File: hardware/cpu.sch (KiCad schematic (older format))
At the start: 6 parts

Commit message: Partial updates for hardware revision 2
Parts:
- removed U?: 74HCT245, symbol 74xx:74HC245
- removed U?: 74AC573, symbol 74xx:74LS573
- removed U?: CAD2, Package_DIP:DIP-24_W7.62mm_Socket, symbol custom_chips:CAD
- removed U?: CID, Package_DIP:DIP-24_W7.62mm_Socket, symbol custom_chips:CBD
- added C? (x5): 0.1uf, symbol Device:C_Small
- added J?: JTAG, Connector_IDC:IDC-Header_2x05_P2.54mm_Vertical, symbol Connector:Conn_ARM_JTAG_SWD_10
- added U? (x3): SN74HC21N, symbol 74xx:74LS21
- added U?: CSC, Package_QFP:TQFP-44_10x10mm_P0.8mm, symbol custom_chips:CSC
- RN?: value R_Network06_US -> 4607X-101-332LF
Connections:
- net labels added: +3V3, R~W, SPI65_TDI, TCK, TDI, TDO, TMS, ~ABORT, ~INTR1, ~INTR2, ~INTR3, ~INTR4, ~IOSEL1, ~IOSEL2, ~IOSEL3, ~IOSEL4, ~IRQ, ~NMI, ~RAM1CS, ~RAM2CS, ~RD, ~RESET, ~ROMCS, ~WR, ϕ2
- net labels removed: +5V, A19, A20, A21, A22, A23, ABORT, INTR1B, INTR2B, INTR3B, INTR4B, IO1SELB, IO2SELB, IO3SELB, IO4SELB, IRQ, IRQB, NMI, PHI1, PHI2, RAM1CSB, RAM2CSB, RDB, RESB, RESET, ROMCSB, ROMPROT, ROMWRB, RWB, WRB
- wire segments 128 -> 136
- no-connect marks 4 -> 6
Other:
- moved on the sheet: RN?, U?

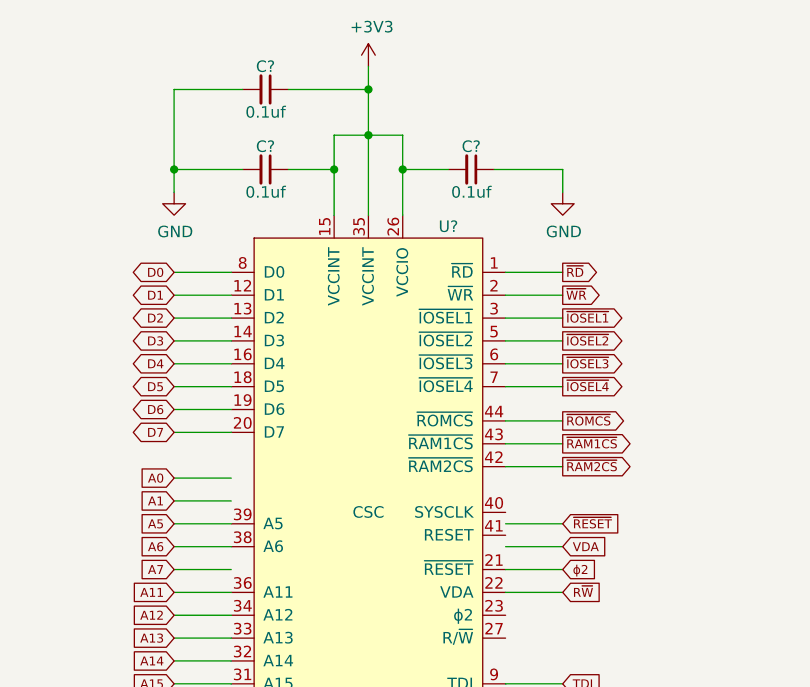
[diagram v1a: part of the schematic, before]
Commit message: Add SPI and missing caps on MAX3232s.
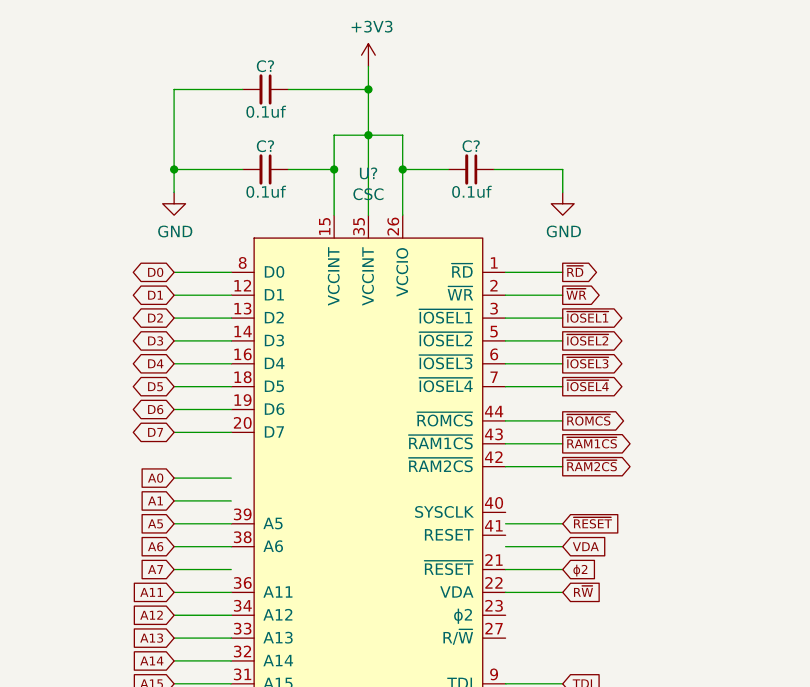
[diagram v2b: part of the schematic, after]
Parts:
- removed U?: CSC, Package_QFP:TQFP-44_10x10mm_P0.8mm, symbol custom_chips:CSC
- added U?: CSC, Package_QFP:TQFP-44_10x10mm_P0.8mm, symbol custom_chips:CSC
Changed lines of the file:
@@
 ~RESET
-$Comp
-L custom_chips:CSC U?
-U 1 1 5DF7979C
-P 6550 2900
-F 0 "U?" H 6900 4150 50  0000 C CNN
-F 1 "CSC" H 6550 2900 50  0000 C CNN
-F 2 "Package_QFP:TQFP-44_10x10mm_P0.8mm" H 6550 2850 50  0001 C CNN
-F 3 "https://www.xilinx.com/support/documentation/data_sheets/ds057.pdf" H 6550 2850 50  0001 C CNN
-	1    6550 2900
-	1    0    0    -1
-$EndComp
 $Comp
 L power:+3V3 #PWR?
@@
 Text GLabel 8850 3650 0    39   Input ~ 0
 TDO
+$Comp
+L custom_chips:CSC U?
+U 1 1 5E4F0787
+P 6550 2900
+F 0 "U?" H 6550 4381 50  0000 C CNN
+F 1 "CSC" H 6550 4290 50  0000 C CNN
+F 2 "Package_QFP:TQFP-44_10x10mm_P0.8mm" H 6550 2850 50  0001 C CNN
+F 3 "https://www.xilinx.com/support/documentation/data_sheets/ds057.pdf" H 6550 2850 50  0001 C CNN
+	1    6550 2900
+	1    0    0    -1
+$EndComp
 $EndSCHEMATC

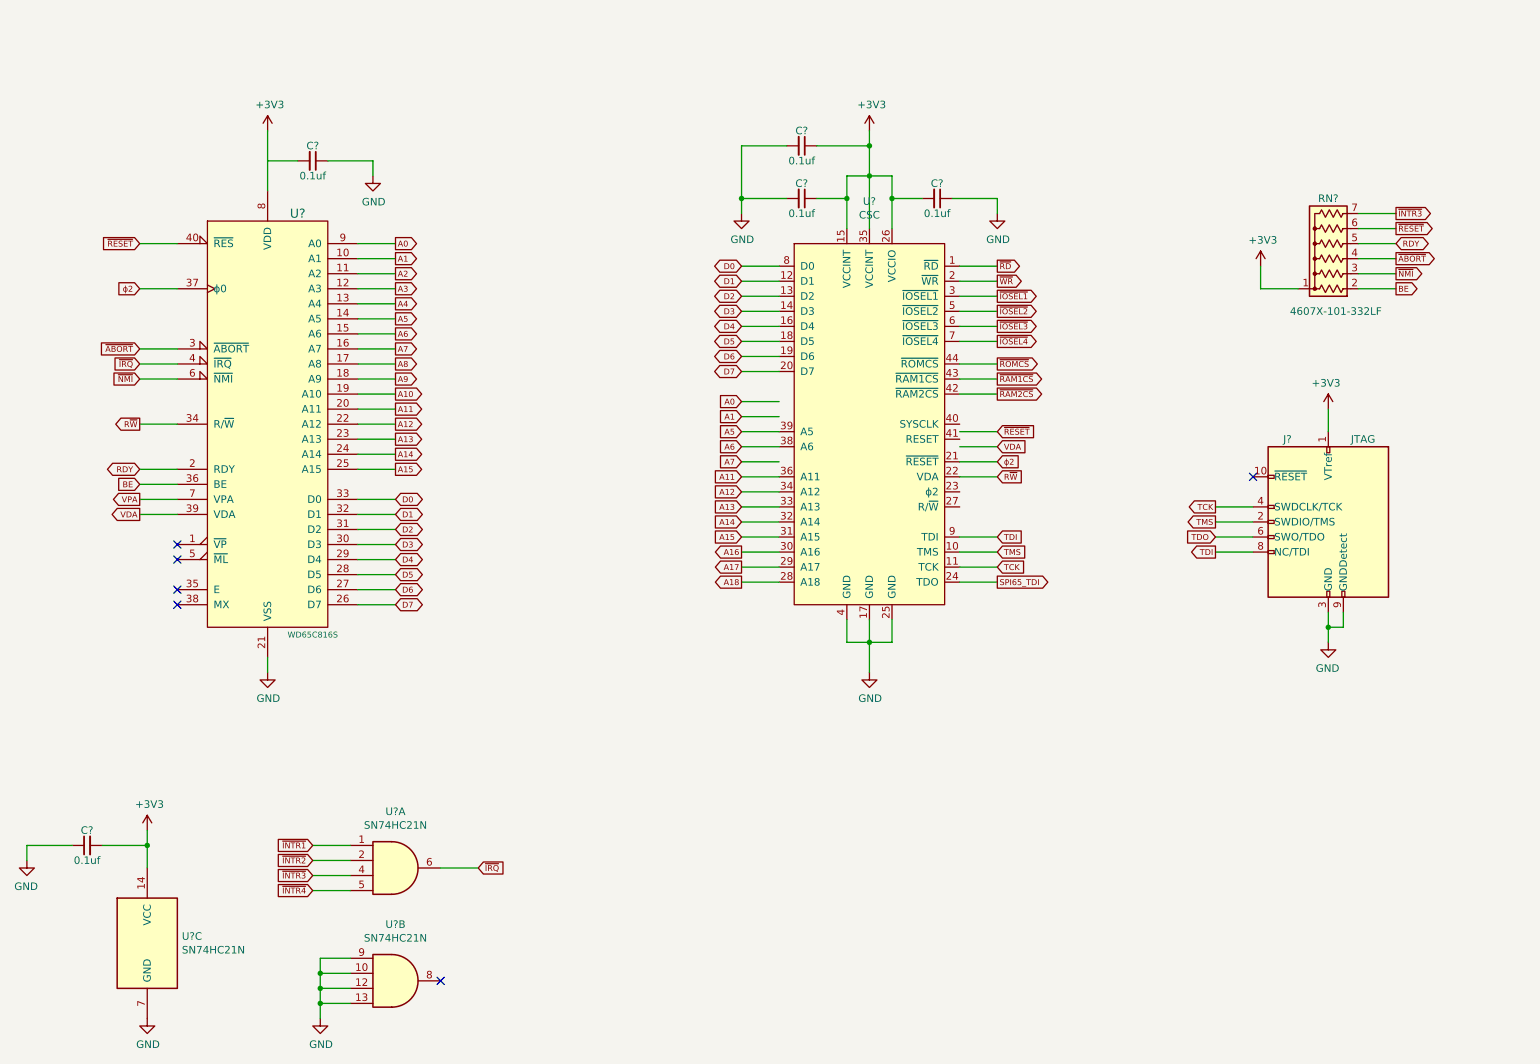
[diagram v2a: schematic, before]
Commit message: Combine VIA, SPI, and UART into a single io.sch sheet. The serial.sch sheet is now just the serial ports and the line drivers.
Add ports.sch sheet for remaining I/O ports.
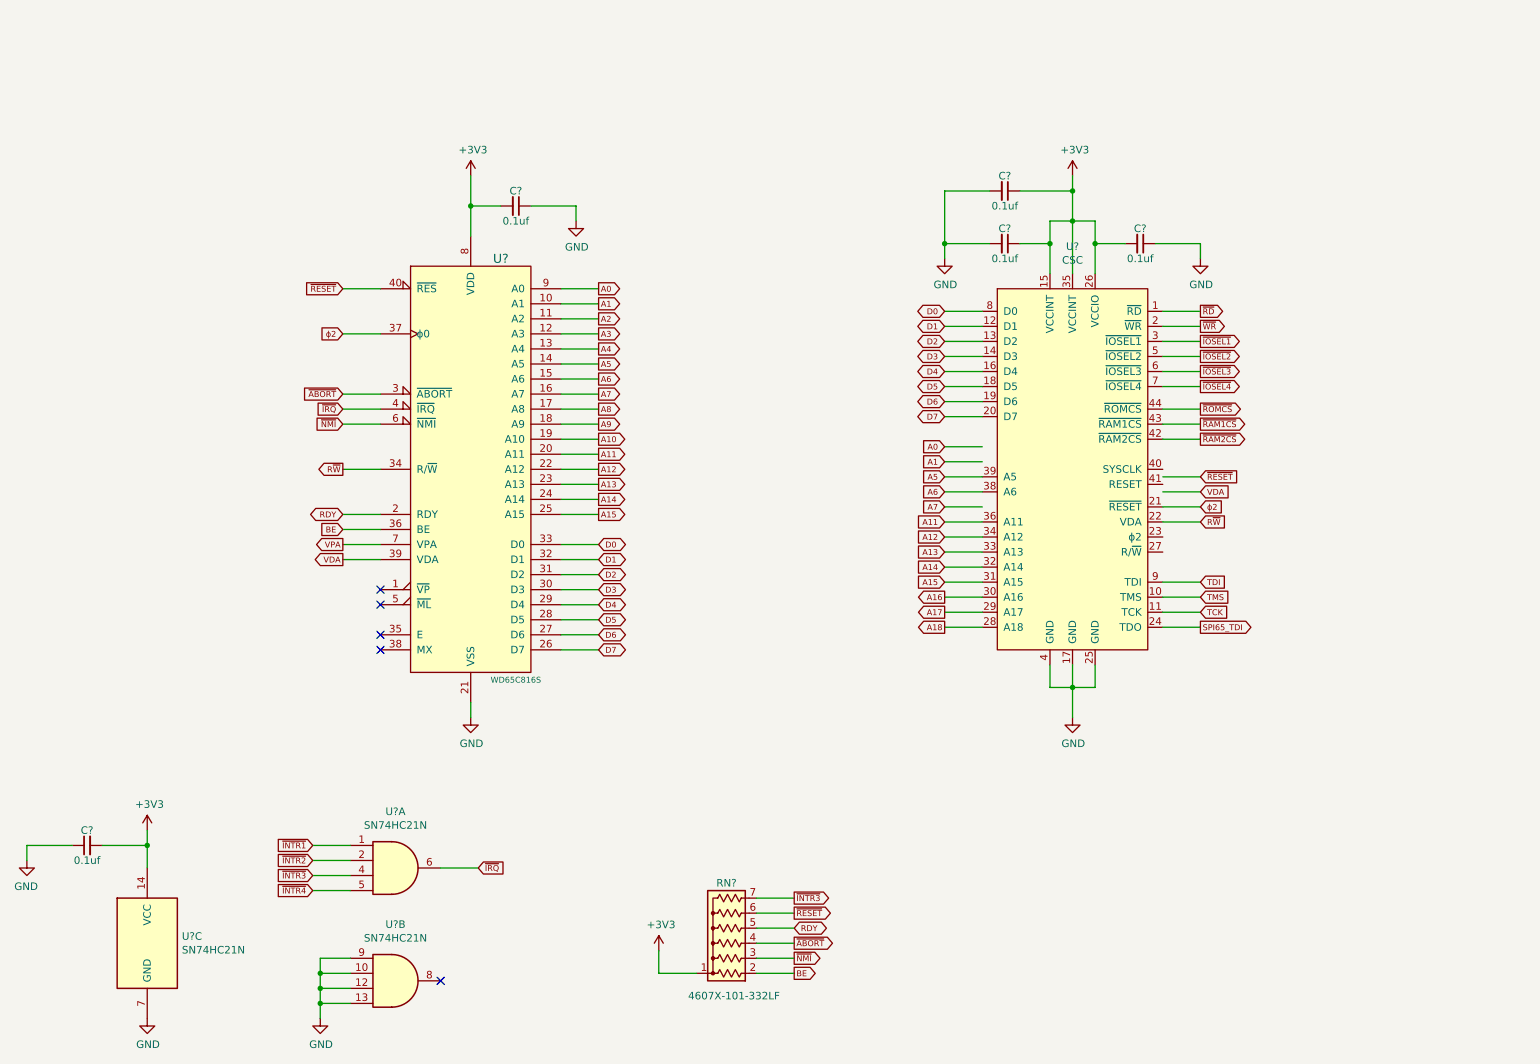
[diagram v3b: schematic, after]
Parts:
- removed J?: JTAG, Connector_IDC:IDC-Header_2x05_P2.54mm_Vertical, symbol Connector:Conn_ARM_JTAG_SWD_10
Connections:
- net labels removed: TDO
- wire segments 136 -> 128
- no-connect marks 6 -> 5
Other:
- moved on the sheet: C?, RN?, U?

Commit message: Latest schematic
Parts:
- RN?: value 4607X-101-332LF -> 4608X-101-332LF; footprint Resistor_THT:R_Array_SIP7 -> Resistor_THT:R_Array_SIP8; symbol Device:R_Network06_US -> Device:R_Network07_US
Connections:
- net ~INTR3: now also RN?.8 (R7); no longer RN?.7 (R6)
- new net RESET: RN?.7 (R6)
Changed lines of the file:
@@
 $Descr A4 11693 8268
 encoding utf-8
-Sheet 2 7
+Sheet 2 8
 Title "CPU and System Controller"
 Date ""
@@
 	3300 3700 3050 3700
 $Comp
-L Device:R_Network06_US RN?
+L Device:R_Network07_US RN?
 U 1 1 5BAB6B12
 P 5600 6250
 F 0 "RN?" V 5900 6250 50  0000 C CNN
-F 1 "4607X-101-332LF" V 5150 6200 50  0000 C CNN
-F 2 "Resistor_THT:R_Array_SIP7" V 5975 6250 50  0001 C CNN
+F 1 "4608X-101-332LF" V 5150 6200 50  0000 C CNN
+F 2 "Resistor_THT:R_Array_SIP8" V 5975 6250 50  0001 C CNN
 F 3 "https://www.mouser.com/datasheet/2/54/4600x-776645.pdf" H 5600 6250 50  0001 C CNN
 	1    5600 6250
 	0    -1   -1   0
 $EndComp
-Text GLabel 6050 6050 2    39   Output ~ 0
+Text GLabel 6050 5950 2    39   Output ~ 0
 ~INTR3
 Wire Wire Line
-	5800 6050 6050 6050
+	5800 5950 6050 5950
 $Comp
 L power:GND #PWR?
@@
 Wire Wire Line
 	3900 1450 3900 1650
+Wire Wire Line
+	5800 6050 6050 6050
+Text GLabel 6050 6050 2    39   Output ~ 0
+RESET
 $EndSCHEMATC

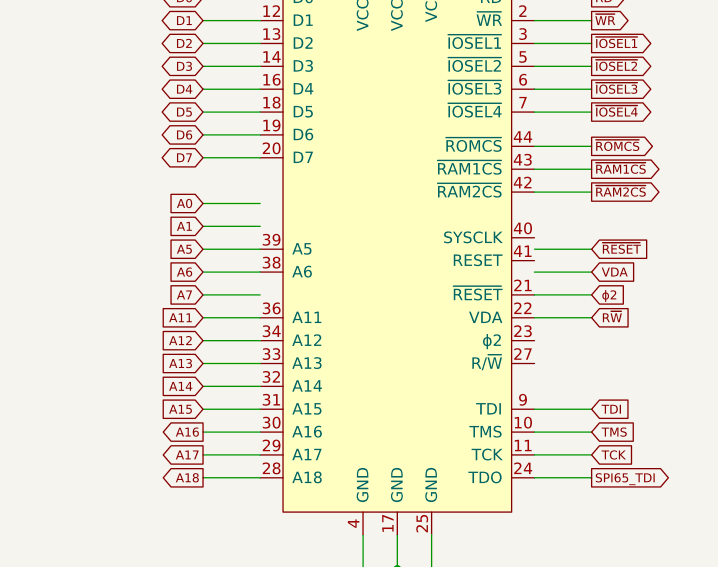
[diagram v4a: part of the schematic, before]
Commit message: More schematic updates to match current prototype build
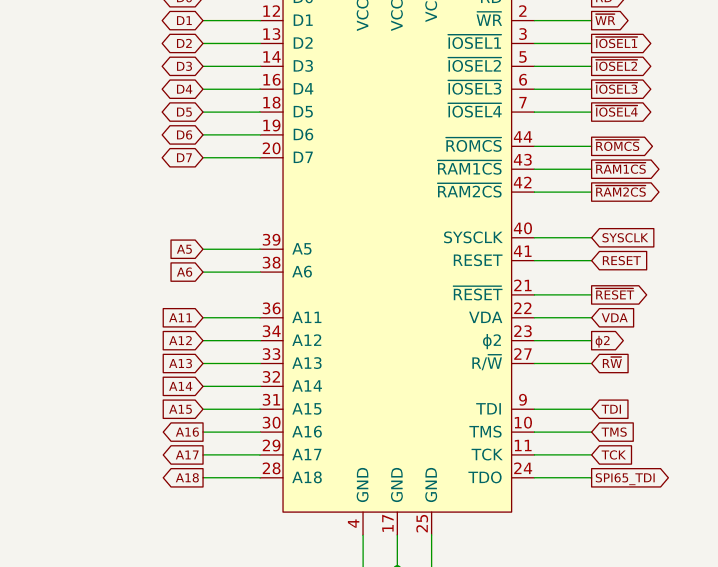
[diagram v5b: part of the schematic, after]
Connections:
- net A7: no longer U?.37 (unused)
- net RESET: now also U?.41 (RESET)
- net R~W: now also U?.27 (R/~W); no longer U?.22 (VDA)
- net VDA: now also U?.22 (VDA)
- net ~RESET: now also U?.21 (~RESET)
- net ϕ2: now also U?.23 (ϕ2); no longer U?.21 (~RESET)
- net SYSCLK: now reaches U?.40 (SYSCLK)
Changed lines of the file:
@@
 EESchema Schematic File Version 4
-LIBS:cole-2-cache
 EELAYER 30 0
 EELAYER END
@@
 Text GLabel 7050 3850 0    39   Input ~ 0
 A14
-Text GLabel 8750 3450 2    39   Input ~ 0
+Text GLabel 8750 3650 2    39   Output ~ 0
 ϕ2
 Wire Wire Line
-	8750 3450 8500 3450
-Text GLabel 8750 3350 2    39   Input ~ 0
+	8750 3650 8500 3650
+Text GLabel 8750 3550 2    39   Input ~ 0
 VDA
 Wire Wire Line
-	8750 3350 8500 3350
-Text GLabel 8750 3550 2    39   Input ~ 0
+	8750 3550 8500 3550
+Text GLabel 8750 3750 2    39   Input ~ 0
 R~W
 Wire Wire Line
-	8750 3550 8500 3550
+	8750 3750 8500 3750
 Text GLabel 8750 2800 2    39   Output ~ 0
 ~ROMCS
@@
 Wire Wire Line
 	7050 3350 7300 3350
-Wire Wire Line
-	7050 3450 7300 3450
 Text GLabel 7050 3350 0    39   Input ~ 0
 A6
-Text GLabel 7050 3450 0    39   Input ~ 0
-A7
 Text GLabel 3950 5850 2    39   Input ~ 0
 ~IRQ
@@
 Wire Wire Line
 	7050 2850 7300 2850
-Text GLabel 7050 3050 0    39   Input ~ 0
-A0
-Wire Wire Line
-	7050 3050 7300 3050
-Wire Wire Line
-	7050 3150 7300 3150
-Text GLabel 7050 3150 0    39   Input ~ 0
-A1
 $Comp
 L power:GND #PWR?
@@
 	0    1    1    0
 $EndComp
-Text GLabel 8750 3250 2    39   Input ~ 0
+Text GLabel 8750 3450 2    39   Output ~ 0
 ~RESET
 Wire Wire Line
-	8750 3250 8500 3250
+	8750 3450 8500 3450
 Wire Wire Line
 	8500 2650 8750 2650
@@
 Text GLabel 6050 6050 2    39   Output ~ 0
 RESET
+Text GLabel 8750 3300 2    39   Input ~ 0
+RESET
+Wire Wire Line
+	8750 3300 8500 3300
+Text GLabel 8750 3200 2    39   Input ~ 0
+SYSCLK
+Wire Wire Line
+	8750 3200 8500 3200
 $EndSCHEMATC
